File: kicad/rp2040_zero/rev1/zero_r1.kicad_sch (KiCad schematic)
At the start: 13 parts, among them J1 jtag, J2 Conn_01x03_Socket, J5 Debug port, U1 RP2040-Zero, U3 3V->VTREF, U4 VTREF->3V, U5 VTREF<->3V, U6 RT9013-33GB

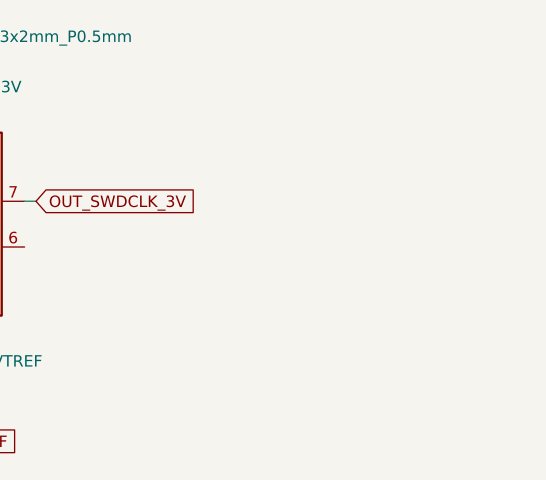
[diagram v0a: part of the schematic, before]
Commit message: kicad : add debug port for rp2xxx carrier board
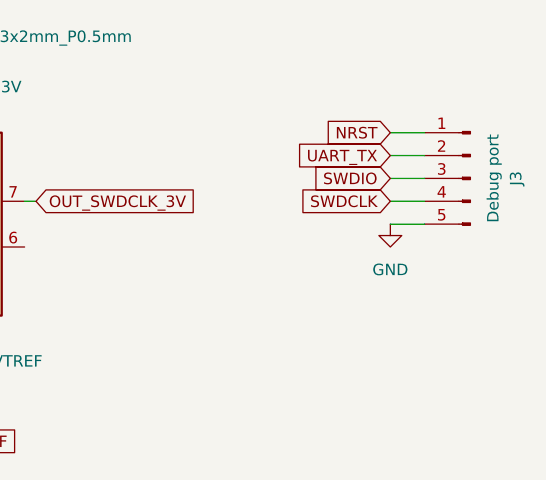
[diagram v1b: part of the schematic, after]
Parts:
- added J3: Debug port, Connector_PinHeader_1.00mm:PinHeader_1x05_P1.00mm_Vertical, symbol Connector:Conn_01x05_Male
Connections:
- net GND: now also J3.5 (Pin_5)
- new net NRST: J3.1 (Pin_1)
- new net SWDCLK: J3.4 (Pin_4)
- new net SWDIO: J3.3 (Pin_3)
- new net UART_TX: J3.2 (Pin_2)
